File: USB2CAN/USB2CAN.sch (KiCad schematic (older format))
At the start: 39 parts, among them J1 USB_C_Receptacle_USB2.0, J2 DB9, J3 SWD, SW1 SW_SPDT, U1 MCP2551, U2 LD1117S33CTR, U3 STM32F302C8Tx, Y1 8mHz

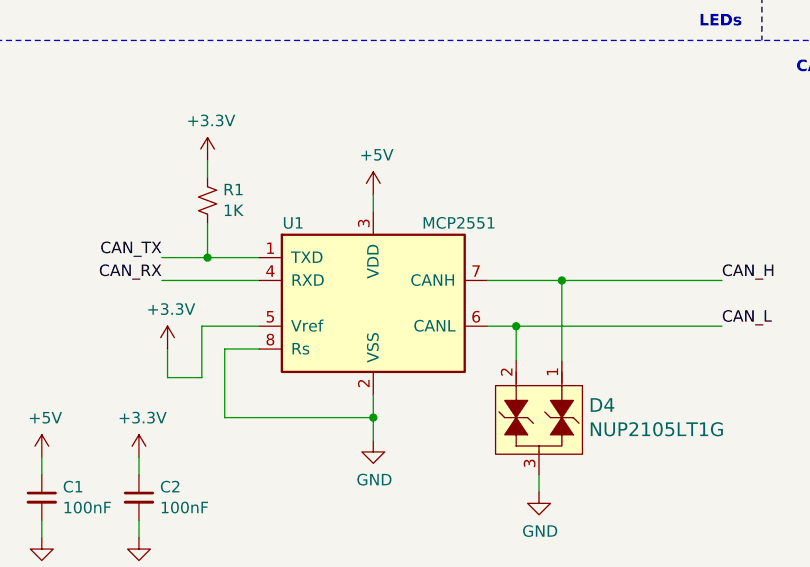
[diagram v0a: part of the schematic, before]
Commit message: Swapped MCP2551 to MCP2562
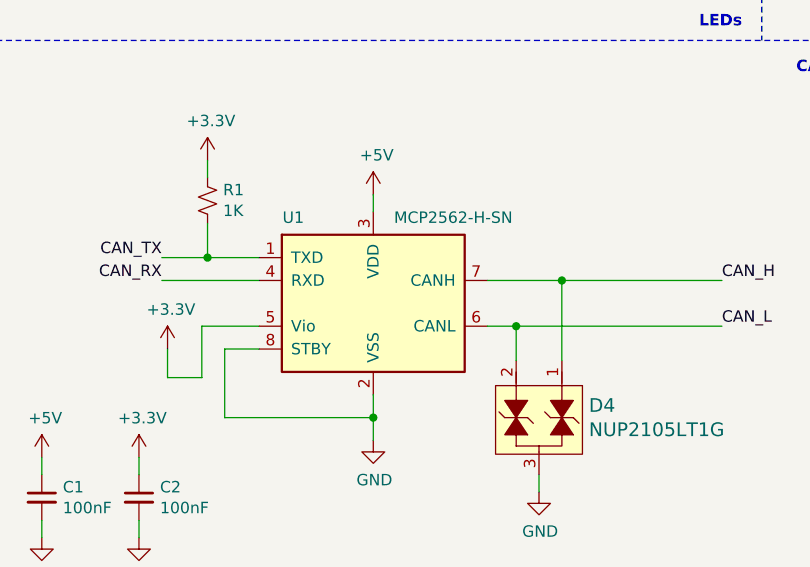
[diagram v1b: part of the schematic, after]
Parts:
- removed U1: MCP2551, Package_SO:SOIC-8_3.9x4.9mm_P1.27mm, symbol Interface_CAN_LIN:MCP2551-I-SN
- added U1: MCP2562-H-SN, Package_SO:SOIC-8_3.9x4.9mm_P1.27mm, symbol Interface_CAN_LIN:MCP2562-H-SN
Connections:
- net +3V3: now also U1.5 (Vio)
- net +5V: now also U1.3 (VDD)
- net CAN_H: now also U1.7 (CANH)
- net CAN_L: now also U1.6 (CANL)
- net CAN_RX: now also U1.4 (RXD)
- net CAN_TX: now also U1.1 (TXD)
- net GND: now also U1.2 (VSS), U1.8 (STBY)
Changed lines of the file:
@@
-$EndComp
-$Comp
-L Interface_CAN_LIN:MCP2551-I-SN U1
-U 1 1 601EC805
-P 2250 6350
-F 0 "U1" H 1900 6700 50  0000 C CNN
-F 1 "MCP2551" H 2625 6700 50  0000 C CNN
-F 2 "Package_SO:SOIC-8_3.9x4.9mm_P1.27mm" H 2250 5850 50  0001 C CIN
-F 3 "http://ww1.microchip.com/downloads/en/devicedoc/21667d.pdf" H 2250 6350 50  0001 C CNN
-F 4 "MCP2551T-I/SNCT-ND" H 2250 6350 50  0001 C CNN "Digi-Key_PN"
-	1    2250 6350
-	1    0    0    -1
 $EndComp
 $Comp
@@
 Wire Wire Line
 	6375 6325 6550 6325
+$Comp
+L Interface_CAN_LIN:MCP2562-H-SN U1
+U 1 1 60A7C9F8
+P 2250 6350
+F 0 "U1" H 1900 6725 50  0000 C CNN
+F 1 "MCP2562-H-SN" H 2600 6725 50  0000 C CNN
+F 2 "Package_SO:SOIC-8_3.9x4.9mm_P1.27mm" H 2250 5850 50  0001 C CIN
+F 3 "http://ww1.microchip.com/downloads/en/DeviceDoc/25167A.pdf" H 2250 6350 50  0001 C CNN
+	1    2250 6350
+	1    0    0    -1
+$EndComp
 $EndSCHEMATC
